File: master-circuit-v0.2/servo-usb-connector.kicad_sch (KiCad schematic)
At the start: 12 parts

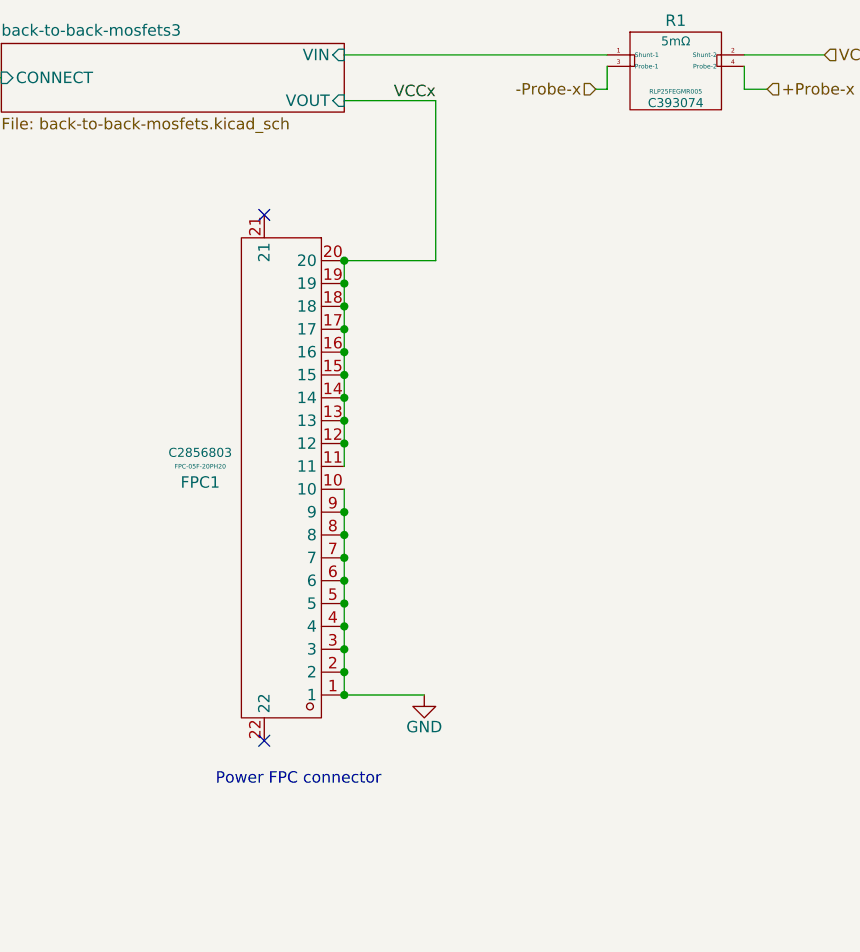
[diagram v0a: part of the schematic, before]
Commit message: Finish extender cable circuit.
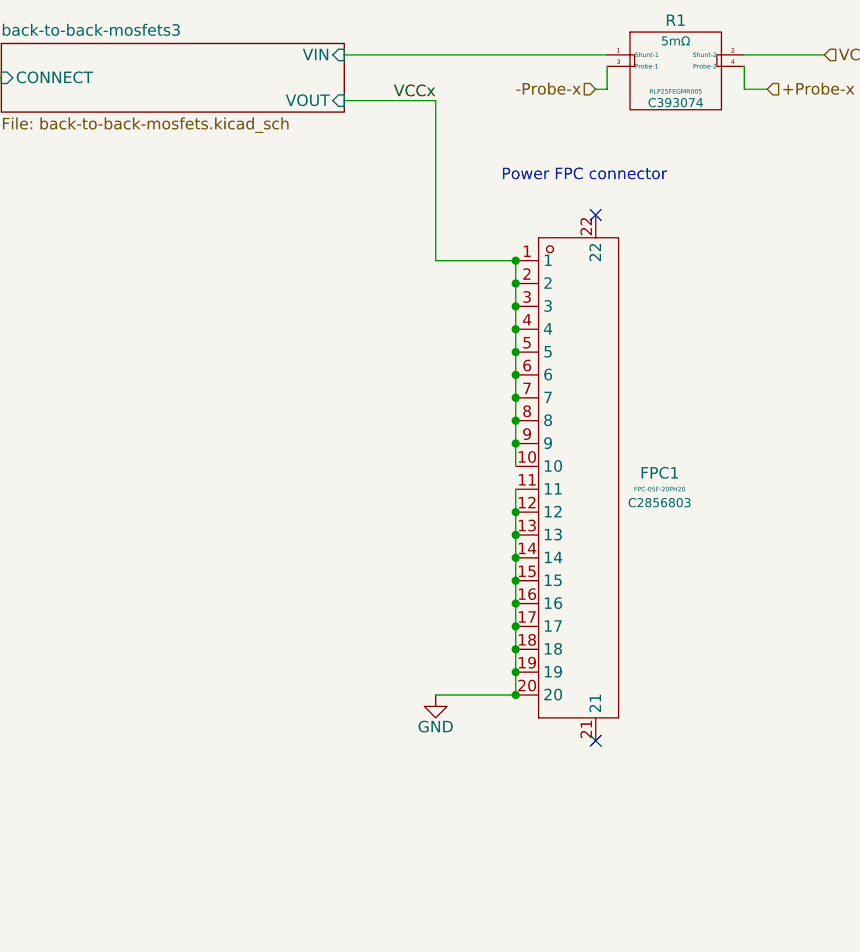
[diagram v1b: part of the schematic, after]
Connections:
- net GND: now also FPC1.11, FPC1.12, FPC1.13, FPC1.14, FPC1.15, FPC1.16, FPC1.17, FPC1.18, FPC1.19, FPC1.20; no longer FPC1.1, FPC1.10, FPC1.2, FPC1.3, FPC1.4, FPC1.5, FPC1.6, FPC1.7, FPC1.8, FPC1.9
- net VCCx: now also FPC1.1, FPC1.10, FPC1.2, FPC1.3, FPC1.4, FPC1.5, FPC1.6, FPC1.7, FPC1.8, FPC1.9; no longer FPC1.11, FPC1.12, FPC1.13, FPC1.14, FPC1.15, FPC1.16, FPC1.17, FPC1.18, FPC1.19, FPC1.20
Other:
- moved on the sheet: FPC1
